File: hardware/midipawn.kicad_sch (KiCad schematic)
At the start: 82 parts, among them J1 MIDI I/O, J10 LOOP 8, J11 LOOP 9, J12 LOOP 10, J13 Barrel_Jack_Switch, J2 I/O, J3 LOOP 1, J4 LOOP 2, J5 LOOP 3, J6 LOOP 4, J7 LOOP 5, J8 LOOP 6, J9 LOOP 7, K1 G6S-2, K10 G6S-2, K2 G6S-2, K3 G6S-2, K4 G6S-2, K5 G6S-2, K6 G6S-2, K7 G6S-2, K8 G6S-2, K9 G6S-2, Q1 2N3904, Q10 2N3904, Q2 2N3904, Q3 2N3904, Q4 2N3904, Q5 2N3904, Q6 2N3904, Q7 2N3904, Q8 2N3904, Q9 2N3904, U1 L7805, U2 6N137

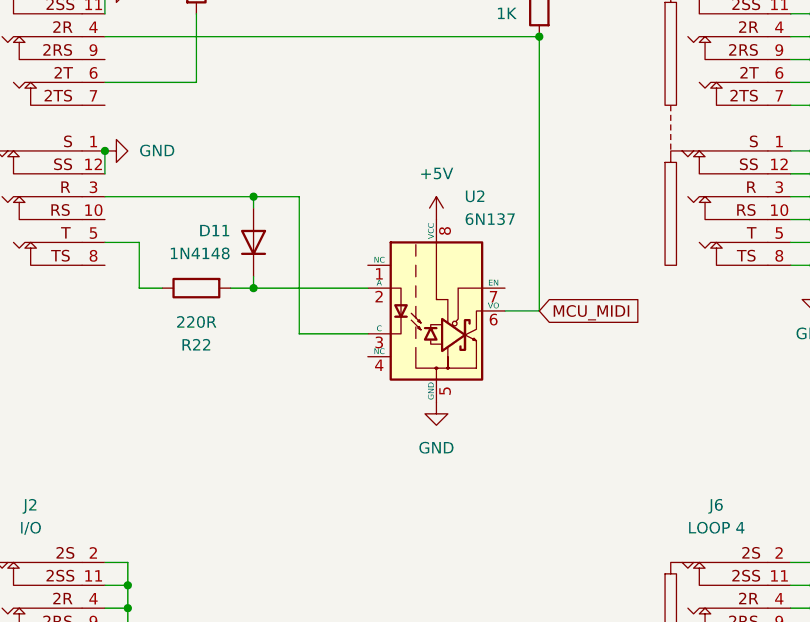
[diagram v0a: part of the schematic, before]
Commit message: Add STEP 3D model for audio jacks connector
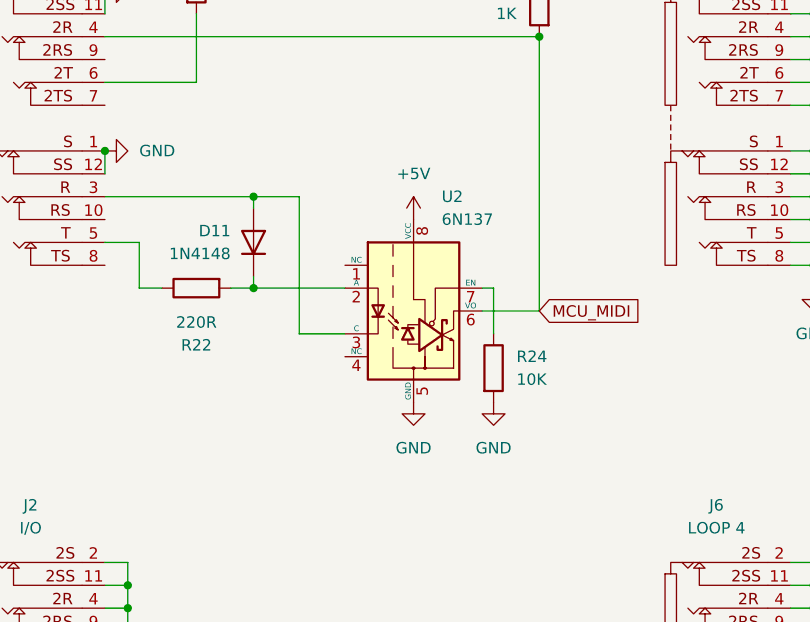
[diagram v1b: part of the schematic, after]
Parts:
- added R24: 10K, Resistor_THT:R_Axial_DIN0204_L3.6mm_D1.6mm_P7.62mm_Horizontal, symbol Device:R
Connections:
- net GND: now also R24.2
- net at U2.7 (EN): now also R24.1
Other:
- moved on the sheet: U2
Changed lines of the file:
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@@
 	(wire
 		(pts
-			(xy 381 96.52) (xy 373.38 96.52)
+			(xy 378.46 96.52) (xy 373.38 96.52)
 		)
 		(stroke
@@
 	(wire
 		(pts
-			(xy 396.24 93.98) (xy 400.05 93.98)
+			(xy 393.7 93.98) (xy 400.05 93.98)
 		)
 		(stroke
@@
 	(wire
 		(pts
-			(xy 368.3 91.44) (xy 381 91.44)
+			(xy 368.3 91.44) (xy 378.46 91.44)
 		)
 		(stroke
@@
 	(wire
 		(pts
+			(xy 393.7 91.44) (xy 394.97 91.44)
+		)
+		(stroke
+			(width 0)
+			(type default)
+		)
+	)
+	(wire
+		(pts
 			(xy 273.05 167.64) (xy 274.32 167.64)
 		)
@@
 	(wire
 		(pts
+			(xy 394.97 91.44) (xy 394.97 96.52)
+		)
+		(stroke
+			(width 0)
+			(type default)
+		)
+	)
+	(wire
+		(pts
 			(xy 523.24 236.22) (xy 523.24 248.92)
 		)
@@
 	(symbol
 		(lib_id "Isolator:6N137")
-		(at 388.62 93.98 0)
+		(at 386.08 93.98 0)
 		(unit 1)
 		(exclude_from_sim no)
@@
 		(fields_autoplaced yes)
 		(property "Reference" "U2"
-			(at 391.7381 81.28 0)
+			(at 389.1981 81.28 0)
 			(effects
 				(font
@@
 		)
 		(property "Value" "6N137"
-			(at 391.7381 83.82 0)
+			(at 389.1981 83.82 0)
 			(effects
 				(font
@@
 		)
 		(property "Footprint" "Package_DIP:DIP-8_W7.62mm"
-			(at 388.62 106.68 0)
+			(at 386.08 106.68 0)
 			(effects
 				(font
@@
 		)
 		(property "Datasheet" "https://docs.broadcom.com/docs/AV02-0940EN"
-			(at 367.03 80.01 0)
+			(at 364.49 80.01 0)
 			(effects
 				(font
@@
 		)
 		(property "Description" "Single High Speed LSTTL/TTL Compatible Optocoupler with enable, dV/dt 1000/us, VCM 10, max 7V VCC, DIP-8"
-			(at 388.62 93.98 0)
+			(at 386.08 93.98 0)
 			(effects
 				(font
@@
 	)
 	(symbol
+		(lib_id "Device:R")
+		(at 394.97 100.33 0)
+		(unit 1)
+		(exclude_from_sim no)
+		(in_bom yes)
+		(on_board yes)
+		(dnp no)
+		(fields_autoplaced yes)
+		(property "Reference" "R24"
+			(at 397.51 99.0599 0)
+			(effects
+				(font
+					(size 1.27 1.27)
+				)
+				(justify left)
+			)
+		)
+		(property "Value" "10K"
+			(at 397.51 101.5999 0)
+			(effects
+				(font
+					(size 1.27 1.27)
+				)
+				(justify left)
+			)
+		)
+		(property "Footprint" "Resistor_THT:R_Axial_DIN0204_L3.6mm_D1.6mm_P7.62mm_Horizontal"
+			(at 393.192 100.33 90)
+			(effects
+				(font
+					(size 1.27 1.27)
+				)
+				(hide yes)
+			)
+		)
+		(property "Datasheet" "~"
+			(at 394.97 100.33 0)
+			(effects
+				(font
+					(size 1.27 1.27)
+				)
+				(hide yes)
+			)
+		)
+		(property "Description" "Resistor"
+			(at 394.97 100.33 0)
+			(effects
+				(font
+					(size 1.27 1.27)
+				)
+				(hide yes)
+			)
+		)
+		(pin "1"
+		)
+		(pin "2"
+		)
+		(instances
+			(project "midipawn"
+				(path "/8c059e4c-6bcb-4300-9e70-551520422cef"
+					(reference "R24")
+					(unit 1)
+				)
+			)
+		)
+	)
+	(symbol
 		(lib_id "power:+9V")
 		(at 99.06 66.04 0)
@@
 	(symbol
 		(lib_id "power:GND")
-		(at 388.62 104.14 0)
+		(at 386.08 104.14 0)
 		(unit 1)
 		(exclude_from_sim no)
@@
 		(fields_autoplaced yes)
 		(property "Reference" "#PWR037"
-			(at 388.62 110.49 0)
+			(at 386.08 110.49 0)
 			(effects
 				(font
@@
 		)
 		(property "Value" "GND"
-			(at 388.62 109.22 0)
+			(at 386.08 109.22 0)
 			(effects
 				(font
@@
 		)
 		(property "Footprint" ""
-			(at 388.62 104.14 0)
+			(at 386.08 104.14 0)
 			(effects
 				(font
@@
 		)
 		(property "Datasheet" ""
-			(at 388.62 104.14 0)
+			(at 386.08 104.14 0)
 			(effects
 				(font
@@
 		)
 		(property "Description" "Power symbol creates a global label with name \"GND\" , ground"
-			(at 388.62 104.14 0)
+			(at 386.08 104.14 0)
 			(effects
 				(font
@@
 	)
 	(symbol
+		(lib_id "power:GND")
+		(at 394.97 104.14 0)
+		(unit 1)
+		(exclude_from_sim no)
+		(in_bom yes)
+		(on_board yes)
+		(dnp no)
+		(fields_autoplaced yes)
+		(property "Reference" "#PWR065"
+			(at 394.97 110.49 0)
+			(effects
+				(font
+					(size 1.27 1.27)
+				)
+				(hide yes)
+			)
+		)
+		(property "Value" "GND"
+			(at 394.97 109.22 0)
+			(effects
+				(font
+					(size 1.27 1.27)
+				)
+			)
+		)
+		(property "Footprint" ""
+			(at 394.97 104.14 0)
+			(effects
+				(font
+					(size 1.27 1.27)
+				)
+				(hide yes)
+			)
+		)
+		(property "Datasheet" ""
+			(at 394.97 104.14 0)
+			(effects
+				(font
+					(size 1.27 1.27)
+				)
+				(hide yes)
+			)
+		)
+		(property "Description" "Power symbol creates a global label with name \"GND\" , ground"
+			(at 394.97 104.14 0)
+			(effects
+				(font
+					(size 1.27 1.27)
+				)
+				(hide yes)
+			)
+		)
+		(pin "1"
+		)
+		(instances
+			(project "midipawn"
+				(path "/8c059e4c-6bcb-4300-9e70-551520422cef"
+					(reference "#PWR065")
+					(unit 1)
+				)
+			)
+		)
+	)
+	(symbol
 		(lib_id "Transistor_BJT:2N3904")
 		(at 219.71 223.52 0)
@@
 	(symbol
 		(lib_id "power:+5V")
-		(at 388.62 83.82 0)
+		(at 386.08 83.82 0)
 		(unit 1)
 		(exclude_from_sim no)
@@
 		(fields_autoplaced yes)
 		(property "Reference" "#PWR036"
-			(at 388.62 87.63 0)
+			(at 386.08 87.63 0)
 			(effects
 				(font
@@
 		)
 		(property "Value" "+5V"
-			(at 388.62 78.74 0)
+			(at 386.08 78.74 0)
 			(effects
 				(font
@@
 		)
 		(property "Footprint" ""
-			(at 388.62 83.82 0)
+			(at 386.08 83.82 0)
 			(effects
 				(font
@@
 		)
 		(property "Datasheet" ""
-			(at 388.62 83.82 0)
+			(at 386.08 83.82 0)
 			(effects
 				(font
@@
 		)
 		(property "Description" "Power symbol creates a global label with name \"+5V\""
-			(at 388.62 83.82 0)
+			(at 386.08 83.82 0)
 			(effects
 				(font

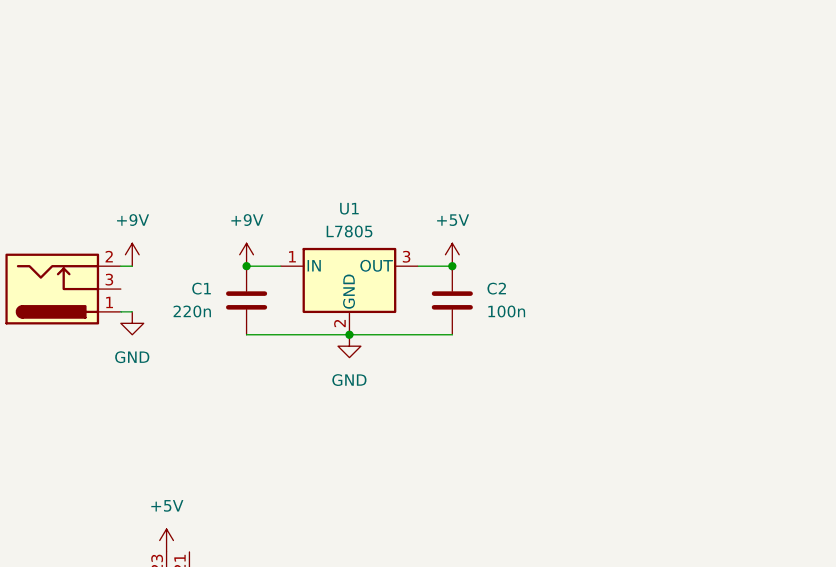
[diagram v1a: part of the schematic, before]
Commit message: Add pull-down resistor on voltage regulator enable pin
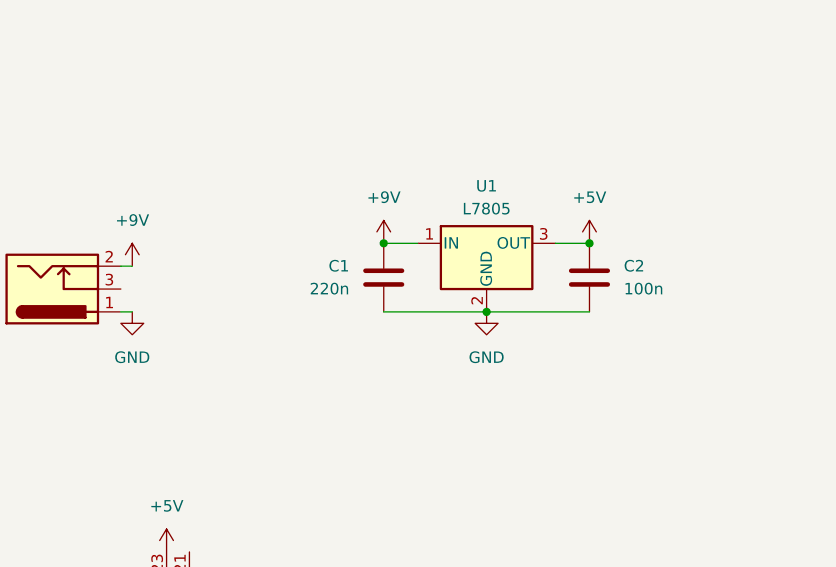
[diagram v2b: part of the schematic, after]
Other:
- moved on the sheet: C1, C2, U1
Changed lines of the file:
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@@
 	)
 	(junction
-		(at 110.49 73.66)
+		(at 125.73 71.12)
 		(diameter 0)
 		(color 0 0 0 0)
@@
 	)
 	(junction
-		(at 99.06 66.04)
+		(at 114.3 63.5)
 		(diameter 0)
 		(color 0 0 0 0)
@@
 	)
 	(junction
-		(at 121.92 66.04)
+		(at 137.16 63.5)
 		(diameter 0)
 		(color 0 0 0 0)
@@
 	(wire
 		(pts
-			(xy 99.06 66.04) (xy 102.87 66.04)
+			(xy 114.3 63.5) (xy 118.11 63.5)
 		)
 		(stroke
@@
 	(wire
 		(pts
-			(xy 118.11 66.04) (xy 121.92 66.04)
+			(xy 133.35 63.5) (xy 137.16 63.5)
 		)
 		(stroke
@@
 	(wire
 		(pts
-			(xy 99.06 73.66) (xy 110.49 73.66)
+			(xy 114.3 71.12) (xy 125.73 71.12)
 		)
 		(stroke
@@
 	(wire
 		(pts
-			(xy 110.49 73.66) (xy 121.92 73.66)
+			(xy 125.73 71.12) (xy 137.16 71.12)
 		)
 		(stroke
@@
 	(symbol
 		(lib_id "Device:C")
-		(at 121.92 69.85 0)
+		(at 137.16 67.31 0)
 		(unit 1)
 		(exclude_from_sim no)
@@
 		(fields_autoplaced yes)
 		(property "Reference" "C2"
-			(at 125.73 68.5799 0)
+			(at 140.97 66.0399 0)
 			(effects
 				(font
@@
 		)
 		(property "Value" "100n"
-			(at 125.73 71.1199 0)
+			(at 140.97 68.5799 0)
 			(effects
 				(font
@@
 		)
 		(property "Footprint" "Capacitor_THT:C_Rect_L7.0mm_W2.5mm_P5.00mm"
-			(at 122.8852 73.66 0)
+			(at 138.1252 71.12 0)
 			(effects
 				(font
@@
 		)
 		(property "Datasheet" "~"
-			(at 121.92 69.85 0)
+			(at 137.16 67.31 0)
 			(effects
 				(font
@@
 		)
 		(property "Description" "Unpolarized capacitor"
-			(at 121.92 69.85 0)
+			(at 137.16 67.31 0)
 			(effects
 				(font
@@
 	(symbol
 		(lib_id "power:+9V")
-		(at 99.06 66.04 0)
+		(at 114.3 63.5 0)
 		(unit 1)
 		(exclude_from_sim no)
@@
 		(fields_autoplaced yes)
 		(property "Reference" "#PWR01"
-			(at 99.06 69.85 0)
+			(at 114.3 67.31 0)
 			(effects
 				(font
@@
 		)
 		(property "Value" "+9V"
-			(at 99.06 60.96 0)
+			(at 114.3 58.42 0)
 			(effects
 				(font
@@
 		)
 		(property "Footprint" ""
-			(at 99.06 66.04 0)
+			(at 114.3 63.5 0)
 			(effects
 				(font
@@
 		)
 		(property "Datasheet" ""
-			(at 99.06 66.04 0)
+			(at 114.3 63.5 0)
 			(effects
 				(font
@@
 		)
 		(property "Description" "Power symbol creates a global label with name \"+9V\""
-			(at 99.06 66.04 0)
+			(at 114.3 63.5 0)
 			(effects
 				(font
@@
 	(symbol
 		(lib_id "Regulator_Linear:L7805")
-		(at 110.49 66.04 0)
+		(at 125.73 63.5 0)
 		(unit 1)
 		(exclude_from_sim no)
@@
 		(fields_autoplaced yes)
 		(property "Reference" "U1"
-			(at 110.49 59.69 0)
+			(at 125.73 57.15 0)
 			(effects
 				(font
@@
 		)
 		(property "Value" "L7805"
-			(at 110.49 62.23 0)
+			(at 125.73 59.69 0)
 			(effects
 				(font
@@
 		)
 		(property "Footprint" "Package_TO_SOT_THT:TO-220-3_Vertical"
-			(at 111.125 69.85 0)
+			(at 126.365 67.31 0)
 			(effects
 				(font
@@
 		)
 		(property "Datasheet" "http://www.st.com/content/ccc/resource/technical/document/datasheet/41/4f/b3/b0/12/d4/47/88/CD00000444.pdf/files/CD00000444.pdf/jcr:content/translations/en.CD00000444.pdf"
-			(at 110.49 67.31 0)
+			(at 125.73 64.77 0)
 			(effects
 				(font
@@
 		)
 		(property "Description" "Positive 1.5A 35V Linear Regulator, Fixed Output 5V, TO-220/TO-263/TO-252"
-			(at 110.49 66.04 0)
+			(at 125.73 63.5 0)
 			(effects
 				(font
@@
 	(symbol
 		(lib_id "Device:C")
-		(at 99.06 69.85 0)
+		(at 114.3 67.31 0)
 		(mirror y)
 		(unit 1)
@@
 		(dnp no)
 		(property "Reference" "C1"
-			(at 95.25 68.5799 0)
+			(at 110.49 66.0399 0)
 			(effects
 				(font
@@
 		)
 		(property "Value" "220n"
-			(at 95.25 71.1199 0)
+			(at 110.49 68.5799 0)
 			(effects
 				(font
@@
 		)
 		(property "Footprint" "Capacitor_THT:C_Rect_L7.0mm_W4.5mm_P5.00mm"
-			(at 98.0948 73.66 0)
+			(at 113.3348 71.12 0)
 			(effects
 				(font
@@
 		)
 		(property "Datasheet" "~"
-			(at 99.06 69.85 0)
+			(at 114.3 67.31 0)
 			(effects
 				(font
@@
 		)
 		(property "Description" "Unpolarized capacitor"
-			(at 99.06 69.85 0)
+			(at 114.3 67.31 0)
 			(effects
 				(font
@@
 	(symbol
 		(lib_id "power:GND")
-		(at 110.49 73.66 0)
+		(at 125.73 71.12 0)
 		(unit 1)
 		(exclude_from_sim no)
@@
 		(fields_autoplaced yes)
 		(property "Reference" "#PWR03"
-			(at 110.49 80.01 0)
+			(at 125.73 77.47 0)
 			(effects
 				(font
@@
 		)
 		(property "Value" "GND"
-			(at 110.49 78.74 0)
+			(at 125.73 76.2 0)
 			(effects
 				(font
@@
 		)
 		(property "Footprint" ""
-			(at 110.49 73.66 0)
+			(at 125.73 71.12 0)
 			(effects
 				(font
@@
 		)
 		(property "Datasheet" ""
-			(at 110.49 73.66 0)
+			(at 125.73 71.12 0)
 			(effects
 				(font
@@
 		)
 		(property "Description" "Power symbol creates a global label with name \"GND\" , ground"
-			(at 110.49 73.66 0)
+			(at 125.73 71.12 0)
 			(effects
 				(font
@@
 	(symbol
 		(lib_id "power:+5V")
-		(at 121.92 66.04 0)
+		(at 137.16 63.5 0)
 		(unit 1)
 		(exclude_from_sim no)
@@
 		(fields_autoplaced yes)
 		(property "Reference" "#PWR05"
-			(at 121.92 69.85 0)
+			(at 137.16 67.31 0)
 			(effects
 				(font
@@
 		)
 		(property "Value" "+5V"
-			(at 121.92 60.96 0)
+			(at 137.16 58.42 0)
 			(effects
 				(font
@@
 		)
 		(property "Footprint" ""
-			(at 121.92 66.04 0)
+			(at 137.16 63.5 0)
 			(effects
 				(font
@@
 		)
 		(property "Datasheet" ""
-			(at 121.92 66.04 0)
+			(at 137.16 63.5 0)
 			(effects
 				(font
@@
 		)
 		(property "Description" "Power symbol creates a global label with name \"+5V\""
-			(at 121.92 66.04 0)
+			(at 137.16 63.5 0)
 			(effects
 				(font
